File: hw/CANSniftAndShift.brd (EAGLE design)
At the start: 160 x 100 mm, 0 parts

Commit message: modified schematics
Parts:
- added C1, C10, C11, C12, C2, C3, C4, C5, C6, C7, C8, C9: 100n, rcl:C0603
- added C13, C14: 18p, rcl:C0603
- added IC1: AT32UC3C264C, AT32UC3C264C:TQFP64
- added Q1: 16MHz, crystal-abracon-abm3-smd:CRYSTAL-ABRACON-ABM7-SMD
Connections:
- new net +3V3: C1.1, C10.1, C2.1, C3.1, C4.1, C5.1, C6.1, C7.1, C8.1, C9.1, IC1.35, IC1.5, IC1.51
- new net +5V: IC1.27
- new net GND: C1.2, C10.2, C11.2, C12.2, C13.2, C14.2, C2.2, C3.2, C4.2, C5.2, C6.2, C7.2, C8.2, C9.2, IC1.17, IC1.26, IC1.30, IC1.36, IC1.52, IC1.6
- new net N$1: C12.1, IC1.18
- new net N$2: C11.1, IC1.29
- new net N$3: C13.1, IC1.31, Q1.P$2
- new net N$4: C14.1, IC1.32, Q1.P$1
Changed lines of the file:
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@@
 </autorouter>
 <elements>
+<element name="IC1" library="AT32UC3C264C" package="TQFP64" value="AT32UC3C264C" x="-8.89" y="8.89"/>
+<element name="C1" library="rcl" package="C0603" value="100n" x="-15.24" y="-2.54"/>
+<element name="C2" library="rcl" package="C0603" value="100n" x="-15.24" y="-7.62"/>
+<element name="C3" library="rcl" package="C0603" value="100n" x="-15.24" y="-12.7"/>
+<element name="C4" library="rcl" package="C0603" value="100n" x="-15.24" y="-17.78"/>
+<element name="C5" library="rcl" package="C0603" value="100n" x="-15.24" y="-22.86"/>
+<element name="C6" library="rcl" package="C0603" value="100n" x="-15.24" y="-27.94"/>
+<element name="C7" library="rcl" package="C0603" value="100n" x="-15.24" y="-33.02"/>
+<element name="C8" library="rcl" package="C0603" value="100n" x="-15.24" y="-38.1"/>
+<element name="C9" library="rcl" package="C0603" value="100n" x="-15.24" y="-43.18"/>
+<element name="C10" library="rcl" package="C0603" value="100n" x="-15.24" y="-48.26"/>
+<element name="C11" library="rcl" package="C0603" value="100n" x="-15.24" y="-58.42"/>
+<element name="C12" library="rcl" package="C0603" value="100n" x="-15.24" y="-63.5"/>
+<element name="Q1" library="crystal-abracon-abm3-smd" package="CRYSTAL-ABRACON-ABM7-SMD" value="16MHz" x="-13.97" y="-68.58"/>
+<element name="C13" library="rcl" package="C0603" value="18p" x="-15.24" y="-73.66"/>
+<element name="C14" library="rcl" package="C0603" value="18p" x="-15.24" y="-77.47"/>
 </elements>
 <signals>
+<signal name="GND">
+<contactref element="C2" pad="2"/>
+<contactref element="C3" pad="2"/>
+<contactref element="C4" pad="2"/>
+<contactref element="C6" pad="2"/>
+<contactref element="C7" pad="2"/>
+<contactref element="C8" pad="2"/>
+<contactref element="C5" pad="2"/>
+<contactref element="C1" pad="2"/>
+<contactref element="C9" pad="2"/>
+<contactref element="C10" pad="2"/>
+<contactref element="IC1" pad="6"/>
+<contactref element="IC1" pad="52"/>
+<contactref element="IC1" pad="36"/>
+<contactref element="IC1" pad="17"/>
+<contactref element="IC1" pad="26"/>
+<contactref element="IC1" pad="30"/>
+<contactref element="C11" pad="2"/>
+<contactref element="C12" pad="2"/>
+<contactref element="C13" pad="2"/>
+<contactref element="C14" pad="2"/>
+<wire x1="-14.39" y1="-73.66" x2="-14.39" y2="-77.47" width="0" layer="19" extent="1-1"/>
+<wire x1="-14.39" y1="-63.5" x2="-14.39" y2="-73.66" width="0" layer="19" extent="1-1"/>
+<wire x1="-14.39" y1="-58.42" x2="-14.39" y2="-63.5" width="0" layer="19" extent="1-1"/>
+<wire x1="-14.39" y1="-48.26" x2="-14.39" y2="-58.42" width="0" layer="19" extent="1-1"/>
+<wire x1="-14.39" y1="-43.18" x2="-14.39" y2="-48.26" width="0" layer="19" extent="1-1"/>
+<wire x1="-14.39" y1="-38.1" x2="-14.39" y2="-43.18" width="0" layer="19" extent="1-1"/>
+<wire x1="-14.39" y1="-33.02" x2="-14.39" y2="-38.1" width="0" layer="19" extent="1-1"/>
+<wire x1="-14.39" y1="-27.94" x2="-14.39" y2="-33.02" width="0" layer="19" extent="1-1"/>
+<wire x1="-14.39" y1="-22.86" x2="-14.39" y2="-27.94" width="0" layer="19" extent="1-1"/>
+<wire x1="-14.39" y1="-17.78" x2="-14.39" y2="-22.86" width="0" layer="19" extent="1-1"/>
+<wire x1="-14.39" y1="-12.7" x2="-14.39" y2="-17.78" width="0" layer="19" extent="1-1"/>
+<wire x1="-14.39" y1="-7.62" x2="-14.39" y2="-12.7" width="0" layer="19" extent="1-1"/>
+<wire x1="-14.39" y1="-2.54" x2="-14.39" y2="-7.62" width="0" layer="19" extent="1-1"/>
+<wire x1="-14.89" y1="1.09" x2="-14.39" y2="-2.54" width="0" layer="19" extent="1-1"/>
+<wire x1="-7.69" y1="1.09" x2="-14.89" y2="1.09" width="0" layer="19" extent="1-1"/>
+<wire x1="-4.49" y1="1.09" x2="-7.69" y2="1.09" width="0" layer="19" extent="1-1"/>
+<wire x1="-1.09" y1="5.29" x2="-4.49" y2="1.09" width="0" layer="19" extent="1-1"/>
+<wire x1="-16.69" y1="10.89" x2="-14.89" y2="1.09" width="0" layer="19" extent="1-1"/>
+<wire x1="-5.29" y1="16.69" x2="-1.09" y2="5.29" width="0" layer="19" extent="1-1"/>
+</signal>
+<signal name="+3V3">
+<contactref element="C8" pad="1"/>
+<contactref element="C7" pad="1"/>
+<contactref element="C6" pad="1"/>
+<contactref element="C5" pad="1"/>
+<contactref element="C4" pad="1"/>
+<contactref element="C3" pad="1"/>
+<contactref element="C2" pad="1"/>
+<contactref element="C1" pad="1"/>
+<contactref element="IC1" pad="5"/>
+<contactref element="IC1" pad="51"/>
+<contactref element="IC1" pad="35"/>
+<contactref element="C9" pad="1"/>
+<contactref element="C10" pad="1"/>
+<wire x1="-16.09" y1="-43.18" x2="-16.09" y2="-48.26" width="0" layer="19" extent="1-1"/>
+<wire x1="-16.09" y1="-38.1" x2="-16.09" y2="-43.18" width="0" layer="19" extent="1-1"/>
+<wire x1="-16.09" y1="-33.02" x2="-16.09" y2="-38.1" width="0" layer="19" extent="1-1"/>
+<wire x1="-16.09" y1="-27.94" x2="-16.09" y2="-33.02" width="0" layer="19" extent="1-1"/>
+<wire x1="-16.09" y1="-22.86" x2="-16.09" y2="-27.94" width="0" layer="19" extent="1-1"/>
+<wire x1="-16.09" y1="-17.78" x2="-16.09" y2="-22.86" width="0" layer="19" extent="1-1"/>
+<wire x1="-16.09" y1="-12.7" x2="-16.09" y2="-17.78" width="0" layer="19" extent="1-1"/>
+<wire x1="-16.09" y1="-7.62" x2="-16.09" y2="-12.7" width="0" layer="19" extent="1-1"/>
+<wire x1="-16.09" y1="-2.54" x2="-16.09" y2="-7.62" width="0" layer="19" extent="1-1"/>
+<wire x1="-16.69" y1="11.69" x2="-16.09" y2="-2.54" width="0" layer="19" extent="1-1"/>
+<wire x1="-4.49" y1="16.69" x2="-16.69" y2="11.69" width="0" layer="19" extent="1-1"/>
+<wire x1="-1.09" y1="4.49" x2="-4.49" y2="16.69" width="0" layer="19" extent="1-1"/>
+</signal>
+<signal name="+5V">
+<contactref element="IC1" pad="27"/>
+</signal>
+<signal name="N$2">
+<contactref element="IC1" pad="29"/>
+<contactref element="C11" pad="1"/>
+<wire x1="-5.29" y1="1.09" x2="-16.09" y2="-58.42" width="0" layer="19" extent="1-1"/>
+</signal>
+<signal name="N$1">
+<contactref element="IC1" pad="18"/>
+<contactref element="C12" pad="1"/>
+<wire x1="-14.09" y1="1.09" x2="-16.09" y2="-63.5" width="0" layer="19" extent="1-1"/>
+</signal>
+<signal name="N$3">
+<contactref element="IC1" pad="31"/>
+<contactref element="Q1" pad="P$2"/>
+<contactref element="C13" pad="1"/>
+<wire x1="-11.82" y1="-68.58" x2="-16.09" y2="-73.66" width="0" layer="19" extent="1-1"/>
+<wire x1="-3.69" y1="1.09" x2="-11.82" y2="-68.58" width="0" layer="19" extent="1-1"/>
+</signal>
+<signal name="N$4">
+<contactref element="IC1" pad="32"/>
+<contactref element="Q1" pad="P$1"/>
+<contactref element="C14" pad="1"/>
+<wire x1="-16.12" y1="-68.58" x2="-16.09" y2="-77.47" width="0" layer="19" extent="1-1"/>
+<wire x1="-2.89" y1="1.09" x2="-16.12" y2="-68.58" width="0" layer="19" extent="1-1"/>
+</signal>
 </signals>
 </board>

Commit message: updated lbr and schematics
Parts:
- added C15, C16: 100n, SchlegelAr_Master:C0402
- added CON4: FCI-10033526-N3212LF, SchlegelAr_Master:FCI-10033526-N3212LF
- added IC7: FT232RL, SchlegelAr_Master:SSOP28
- added R22, R23: 0R, SchlegelAr_Master:R0402
- IC1: value AT32UC3C264C -> (none)
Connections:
- new net +5V_USB: C16.1, CON4.1, IC7.19, IC7.20, IC7.4
- new net FTDI_3V3OUT: C15.1, IC7.17
- new net FTDI_RXD: IC1.58, IC7.5
- new net FTDI_TXD: IC1.59, IC7.1
- new net N$5: IC7.15, R23.2
- new net N$6: IC7.16, R22.2
- new net USB_D+: CON4.3, R23.1
- new net USB_D-: CON4.2, R22.1
- net GND: now also C15.2, C16.2, CON4.5, CON4.GND@1, CON4.GND@2, CON4.GND@3, CON4.GND@4, IC7.18, IC7.21, IC7.25, IC7.26, IC7.7

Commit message: modified lbr
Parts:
- added C17, C18: (no value), SchlegelAr_Master:C0603
- added IC2: (no value), v-reg:78XXL
- added SV1: (no value), con-harting-ml:ML10
- C1, C10, C11, C12, C13, C14, C2, C3, C4, C5, C6, C7, C8, C9: device rcl:C0603 -> SchlegelAr_Master:C0603
- moved C5 111.8 mm to (-15.2, -134.6)
- moved C1 111.8 mm to (-15.2, -114.3)
- moved C2 111.8 mm to (-15.2, -119.4)
- moved C3 111.8 mm to (-15.2, -124.5)
- moved C4 111.8 mm to (-15.2, -129.5)
- moved C6 111.8 mm to (-15.2, -139.7)
- moved C7 106.8 mm to (-10.2, -139.7)
- moved C12 106.7 mm to (-15.2, -170.2)
- moved C8 106.7 mm to (-15.2, -144.8)
- moved C11 106.7 mm to (-15.2, -165.1)
- moved C9 101.7 mm to (-10.2, -144.8)
- moved C10 101.6 mm to (-15.2, -149.9)
- moved C14 82.6 mm to (-15.2, -160.0)
- moved C13 81.3 mm to (-15.2, -154.9)
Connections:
- new net !RESET: IC1.64
- new net +12V: C18.2, IC2.IN
- new net CAN0RX: IC1.45
- new net CAN0TX: IC1.46
- new net JTAG_TCK: IC1.1, SV1.1
- new net JTAG_TDI: IC1.2, SV1.9
- new net JTAG_TDO: IC1.3, SV1.3
- new net JTAG_TMS: IC1.4, SV1.5
- new net N$13: SV1.6
- new net USB_DM: IC1.24
- new net USB_DP: IC1.25
- new net USB_VBUS: IC1.23
- net +3V3: now also C1.2, C17.2, C2.2, C3.2, C4.2, C5.2, IC2.OUT, SV1.4; no longer C1.1, C10.1, C2.1, C3.1, C4.1, C5.1, C6.1, C7.1, C8.1, C9.1
- net GND: now also C1.1, C11.1, C12.1, C13.1, C14.1, C17.1, C18.1, C2.1, C3.1, C4.1, C5.1, IC2.GND, SV1.10, SV1.2; no longer C1.2, C10.2, C11.2, C12.2, C13.2, C14.2, C2.2, C3.2, C4.2, C5.2, C6.2, C7.2, C8.2, C9.2
- net N$1: now also C12.2; no longer C12.1
- net N$2: now also C11.2; no longer C11.1
- net N$3: now also C13.2; no longer C13.1
- net N$4: now also C14.2; no longer C14.1

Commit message: first version of schematic
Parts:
- removed C18: (no value), SchlegelAr_Master:C0603
- removed IC2: (no value), v-reg:78XXL
- added C19, C20: (no value), SchlegelAr_Master:C0603
- added CON1: FCI-10033526-N3212LF, SchlegelAr_Master:FCI-10033526-N3212LF
- added IC3, IC4: (no value), SchlegelAr_Master:SO8
- added IC5: (no value), v-reg:78XXL
- added JP1, JP2, JP3: JUMPER2, SchlegelAr_Master:JUMPER2_THROUGHHOLE
- added R1: (no value), SchlegelAr_Master:R0603
- added R2, R3: 120R, SchlegelAr_Master:R0603
- added S1: (no value), switch-omron:B3F-10XX
- added X1, X2: (no value), con-subd:F09HP
- C17: value (none) -> 10u; device SchlegelAr_Master:C0603 -> SchlegelAr_Master:C_POL_4X4MM
- moved C17 139.4 mm to (-74.9, -306.1)
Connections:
- removed net +3V3: C1.2, C17.2, C2.2, C3.2, C4.2, C5.2, IC1.35, IC1.5, IC1.51, IC2.OUT, SV1.4
- removed net +5V_USB: C16.1, CON4.1, IC7.19, IC7.20, IC7.4
- removed net N$13: SV1.6
- new net CAN1RX: IC1.39, IC4.4
- new net CAN1TX: IC1.40, IC4.1
- new net CANH0: IC3.7, JP2.1, X1.7
- new net CANH1: IC4.7, JP3.1, X2.7
- new net CANL0: IC3.6, R2.1, X1.2
- new net CANL1: IC4.6, R3.1, X2.2
- new net N$12: C16.1, IC7.20
- new net N$7: JP2.2, R2.2
- new net N$9: JP3.2, R3.2
- new net SPI0_MISO: IC1.48
- new net SPI0_MOSI: IC1.47
- new net SPI0_NPCS0: IC1.50
- new net SPI0_SCK: IC1.49
- net !RESET: now also R1.1, S1.3, S1.4, SV1.6
- net +12V: now also C20.2, IC5.IN; no longer C18.2, IC2.IN
- net +5V: now also C1.2, C10.2, C17.+, C19.2, C2.2, C3.2, C4.2, C5.2, C6.2, C7.2, C8.2, C9.2, CON4.1, IC1.35, IC1.5, IC1.51, IC3.3, IC4.3, IC5.OUT, IC7.19, IC7.4, JP1.2, R1.2, SV1.4
- net CAN0RX: now also IC3.4
- net CAN0TX: now also IC3.1
- net GND: now also C10.1, C17.-, C19.1, C20.1, C6.1, C7.1, C8.1, C9.1, CON1.5, CON1.GND@1, CON1.GND@2, CON1.GND@3, CON1.GND@4, IC3.2, IC3.8, IC4.2, IC4.8, IC5.GND, S1.1, S1.2; no longer C17.1, C18.1, IC2.GND
- net USB_DM: now also CON1.2
- net USB_DP: now also CON1.3
- net USB_VBUS: now also CON1.1, JP1.1

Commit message: updated sch
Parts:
- added D1: Z3V6, SchlegelAr_Master:DO214A
- C13, C14: value 18p -> 27p
- IC3, IC4: value (none) -> TJA1050
- R1: value (none) -> 10k
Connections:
- new net N$8: D1.A, IC1.28
- net +5V: now also D1.C
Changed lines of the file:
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@@
 <element name="C9" library="SchlegelAr_Master" package="C0603" value="100n" x="-10.16" y="-144.78"/>
 <element name="C10" library="SchlegelAr_Master" package="C0603" value="100n" x="-15.24" y="-149.86"/>
-<element name="C13" library="SchlegelAr_Master" package="C0603" value="18p" x="-15.24" y="-154.94"/>
-<element name="C14" library="SchlegelAr_Master" package="C0603" value="18p" x="-15.24" y="-160.02"/>
+<element name="C13" library="SchlegelAr_Master" package="C0603" value="27p" x="-15.24" y="-154.94"/>
+<element name="C14" library="SchlegelAr_Master" package="C0603" value="27p" x="-15.24" y="-160.02"/>
 <element name="C11" library="SchlegelAr_Master" package="C0603" value="100n" x="-15.24" y="-165.1"/>
 <element name="C12" library="SchlegelAr_Master" package="C0603" value="100n" x="-15.24" y="-170.18"/>
@@
 <attribute name="OC_FARNELL" value="176432" x="-41.91" y="-198.12" size="1.778" layer="27" display="off"/>
 </element>
-<element name="R1" library="SchlegelAr_Master" package="R0603" value="" x="-44.45" y="-207.01"/>
-<element name="IC3" library="SchlegelAr_Master" package="SO8" value="" x="-41.91" y="-213.36"/>
-<element name="IC4" library="SchlegelAr_Master" package="SO8" value="" x="-41.91" y="-222.25"/>
+<element name="R1" library="SchlegelAr_Master" package="R0603" value="10k" x="-44.45" y="-207.01"/>
+<element name="IC3" library="SchlegelAr_Master" package="SO8" value="TJA1050" x="-41.91" y="-213.36"/>
+<element name="IC4" library="SchlegelAr_Master" package="SO8" value="TJA1050" x="-41.91" y="-222.25"/>
 <element name="IC5" library="v-reg" package="78XXL" value="" x="-41.91" y="-242.57"/>
 <element name="C19" library="SchlegelAr_Master" package="C0603" value="" x="-34.29" y="-228.6"/>
@@
 <element name="R3" library="SchlegelAr_Master" package="R0603" value="120R" x="-67.31" y="-308.61"/>
 <element name="C17" library="SchlegelAr_Master" package="C_POL_4X4MM" value="10u" x="-74.93" y="-306.07"/>
+<element name="D1" library="SchlegelAr_Master" package="DO214A" value="Z3V6" x="-73.66" y="-314.96"/>
 </elements>
 <signals>
@@
 <contactref element="C19" pad="2"/>
 <contactref element="C17" pad="+"/>
+<contactref element="D1" pad="C"/>
 <wire x1="-41.275" y1="-216.4334" x2="-43.6" y2="-207.01" width="0" layer="19" extent="1-1"/>
 <wire x1="-41.275" y1="-225.3234" x2="-41.275" y2="-216.4334" width="0" layer="19" extent="1-1"/>
@@
 <wire x1="-13.03" y1="-81.75" x2="-8.535" y2="-92.895" width="0" layer="19" extent="1-1"/>
 <wire x1="-73.13" y1="-306.07" x2="-39.37" y2="-246.38" width="0" layer="19" extent="1-1"/>
+<wire x1="-76.21" y1="-314.96" x2="-73.13" y2="-306.07" width="0" layer="19" extent="1-1"/>
 <wire x1="-6.89" y1="1.09" x2="-13.03" y2="-81.75" width="0" layer="19" extent="1-1"/>
 <wire x1="-1.09" y1="4.49" x2="-6.89" y2="1.09" width="0" layer="19" extent="1-1"/>
@@
 <wire x1="-58.42" y1="-297.18" x2="-66.46" y2="-308.61" width="0" layer="19" extent="1-1"/>
 </signal>
+<signal name="N$8">
+<contactref element="IC1" pad="28"/>
+<contactref element="D1" pad="A"/>
+<wire x1="-6.09" y1="1.09" x2="-71.11" y2="-314.96" width="0" layer="19" extent="1-1"/>
+</signal>
 </signals>

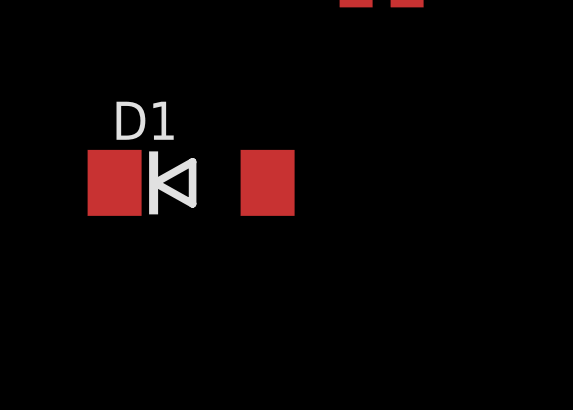
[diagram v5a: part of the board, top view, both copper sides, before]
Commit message: added embedded sw frame, started to work on port driver
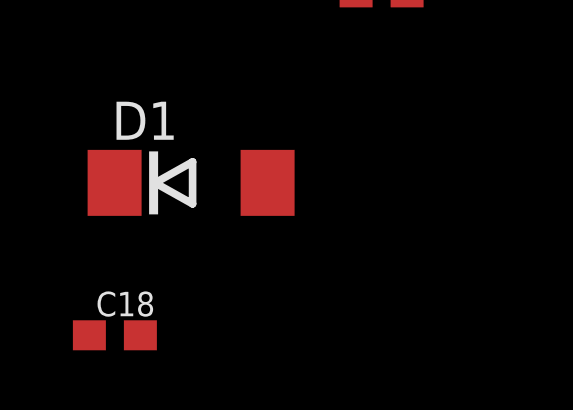
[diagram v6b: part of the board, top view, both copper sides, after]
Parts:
- added C18: 100n, SchlegelAr_Master:C0603
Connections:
- net GND: now also C18.1
- net N$8: now also C18.2
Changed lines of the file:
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@@
 <element name="C17" library="SchlegelAr_Master" package="C_POL_4X4MM" value="10u" x="-74.93" y="-306.07"/>
 <element name="D1" library="SchlegelAr_Master" package="DO214A" value="Z3V6" x="-73.66" y="-314.96"/>
+<element name="C18" library="SchlegelAr_Master" package="C0603" value="100n" x="-76.2" y="-320.04"/>
 </elements>
 <signals>
@@
 <contactref element="C20" pad="1"/>
 <contactref element="C17" pad="-"/>
+<contactref element="C18" pad="1"/>
 <wire x1="-42.545" y1="-216.4334" x2="-43.815" y2="-210.2866" width="0" layer="19" extent="1-1"/>
 <wire x1="-43.815" y1="-219.1766" x2="-42.545" y2="-216.4334" width="0" layer="19" extent="1-1"/>
@@
 <wire x1="-45.3" y1="-250.19" x2="-41.91" y2="-246.38" width="0" layer="19" extent="1-1"/>
 <wire x1="-76.73" y1="-306.07" x2="-45.3" y2="-250.19" width="0" layer="19" extent="1-1"/>
+<wire x1="-77.05" y1="-320.04" x2="-76.73" y2="-306.07" width="0" layer="19" extent="1-1"/>
 <wire x1="-14.89" y1="1.09" x2="-15.88" y2="-81.75" width="0" layer="19" extent="1-1"/>
 <wire x1="-7.69" y1="1.09" x2="-14.89" y2="1.09" width="0" layer="19" extent="1-1"/>
@@
 <contactref element="IC1" pad="28"/>
 <contactref element="D1" pad="A"/>
+<contactref element="C18" pad="2"/>
+<wire x1="-71.11" y1="-314.96" x2="-75.35" y2="-320.04" width="0" layer="19" extent="1-1"/>
 <wire x1="-6.09" y1="1.09" x2="-71.11" y2="-314.96" width="0" layer="19" extent="1-1"/>
 </signal>
